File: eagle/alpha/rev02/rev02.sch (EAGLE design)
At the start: 382 parts, among them CN1 HOST, CN2 HOST, IC1 N25Q128A13ES, IC2 74AC244DW, IC3 N25Q128A13ES, J1 STM32-SWD, Q1 2N7002, Q2 BC818, Q4 2N7002, Q5 ASFL1, Q6 2N7002, T1 BC847, T2 BC847, U1 LMZ13608, U10 ATTINY828R-AU, U11 MC14551BDG, U12 23K640-I/SN, U13 XC7A200TFBG484, U14 EN6347QI, U15 EN6347QI, U16 EN5364QI, U2 LT3060ITS8-15, U3 MC74HC1G14DTT1G, U4 STM32F429BIT6, U5 IS45S32160F, U6 IS45S32160F, U7 MCP79412-I/SN, U8 FT232H_SERIAL, U9 FT232H_SERIAL, Y1 12 MHz, Y2 12 MHz

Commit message: First set of updates based on review feedback.
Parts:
- removed R17: 4.7k, resistor:R-EU_R0402
- C13, C7: value 2.2 uF -> 4.7 uF
- R24, R25, R28, R29: value 220 -> 330
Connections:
- removed net N$53: R4.2, U1.SYNC
- new net N$3: Q5.FO, R4.2
- net FPGA_GCLK: no longer Q5.FO
- net GND: now also C22.1, C23.1, C24.1, C25.1; no longer R17.1, R18.1, R4.1
- net KSM_PROM_CS_N: now also U4IO.PB0
- net VCCO_3V3: now also R18.1; no longer C22.1, C23.1, C24.1, C25.1, R17.2
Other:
- note added: "Connector for external 3V3 battery. Place a jumper between pins 1-2 to "emulate" having a battery present."
- note added: "NOTE: GPIO pins should be length matched to support I/O at XXX MHz (pavel)"
- note added: "NOTE: One of the FPGA_GPIO_* pins should be connected to one of the MRCC pins."
- note added: "XXX Add EEPROM for USB settings. Plan for now is to not populate it on the Alpha though."
- note removed: "Do we need more speed? Joachim expressed that we might need a faster interconnect to the Alpha than the 12 Mbaud the FT232H can deliver in UART mode (in an e-mail to tech@ 2015-08-18). An alternative is to connect all of the ADBUS (and more) to the ARM, and use one of the faster modes this chip supports (fastest: synchronous FT245 parallel FIFO at 40 Mbyte/s). Enabling the faster modes requires t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"
- note removed: "FPGA_GPIO_B* is blue LEDs in Alpha block diagram. Suggest pin header instead for more versatility."
- note removed: "Place a jumper between pins 1-2 to "emulate" having a battery present."
- note removed: "XXX EEPROM for USB settings or not?"
- moved on the sheet: C100, C101, C104, C113, C114, C115, C116, C117, C118, C119, C120, C123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

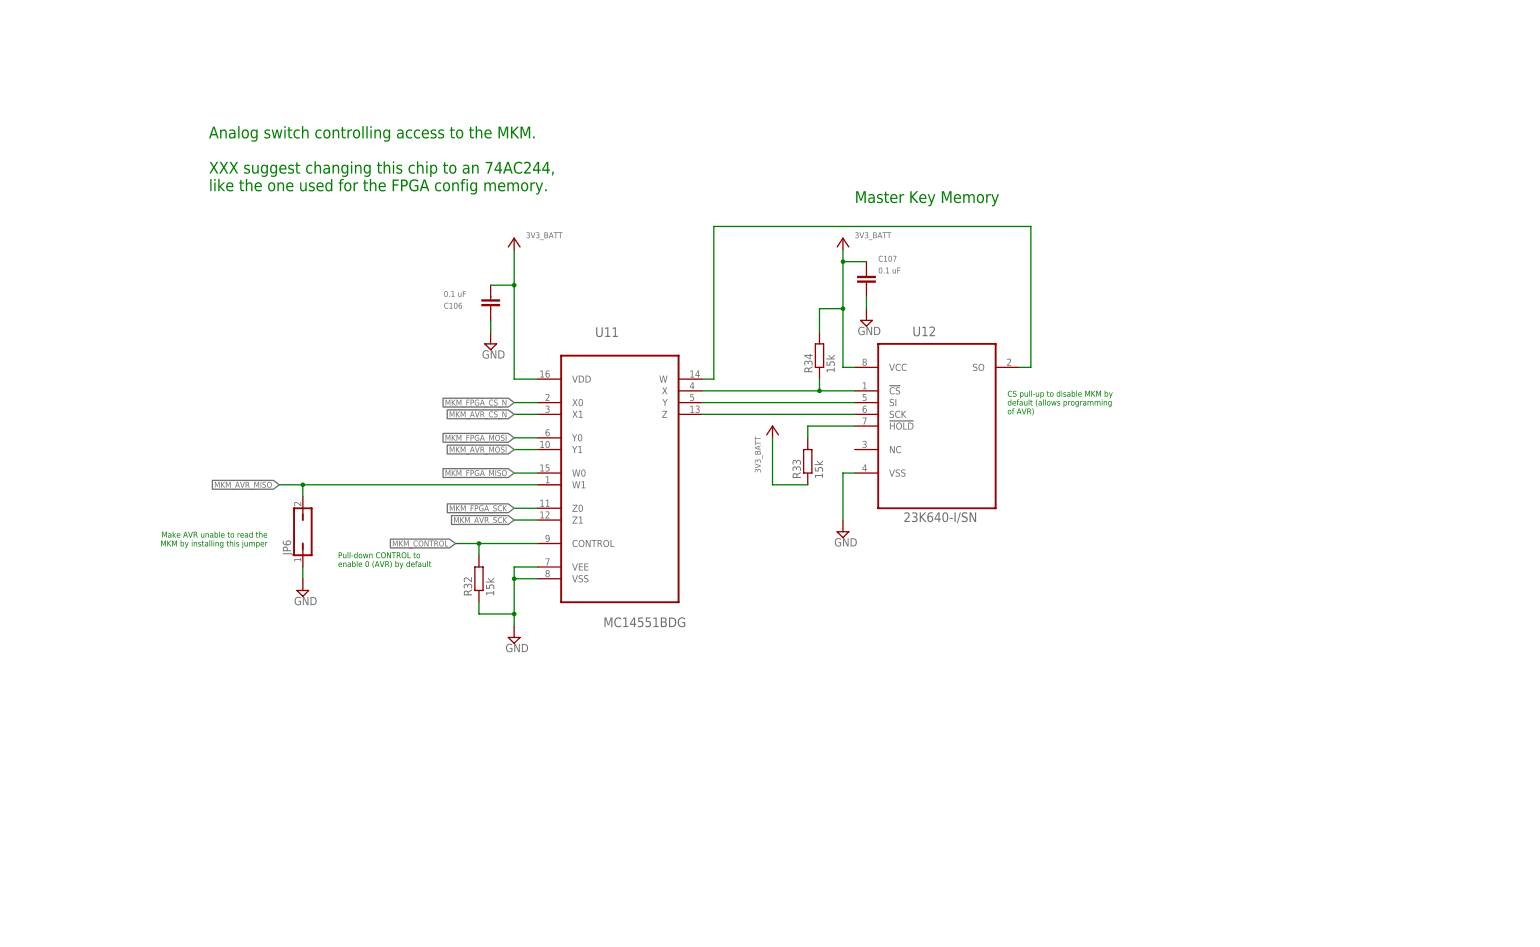
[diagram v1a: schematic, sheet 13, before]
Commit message: More schematic updates after review with Pavel.
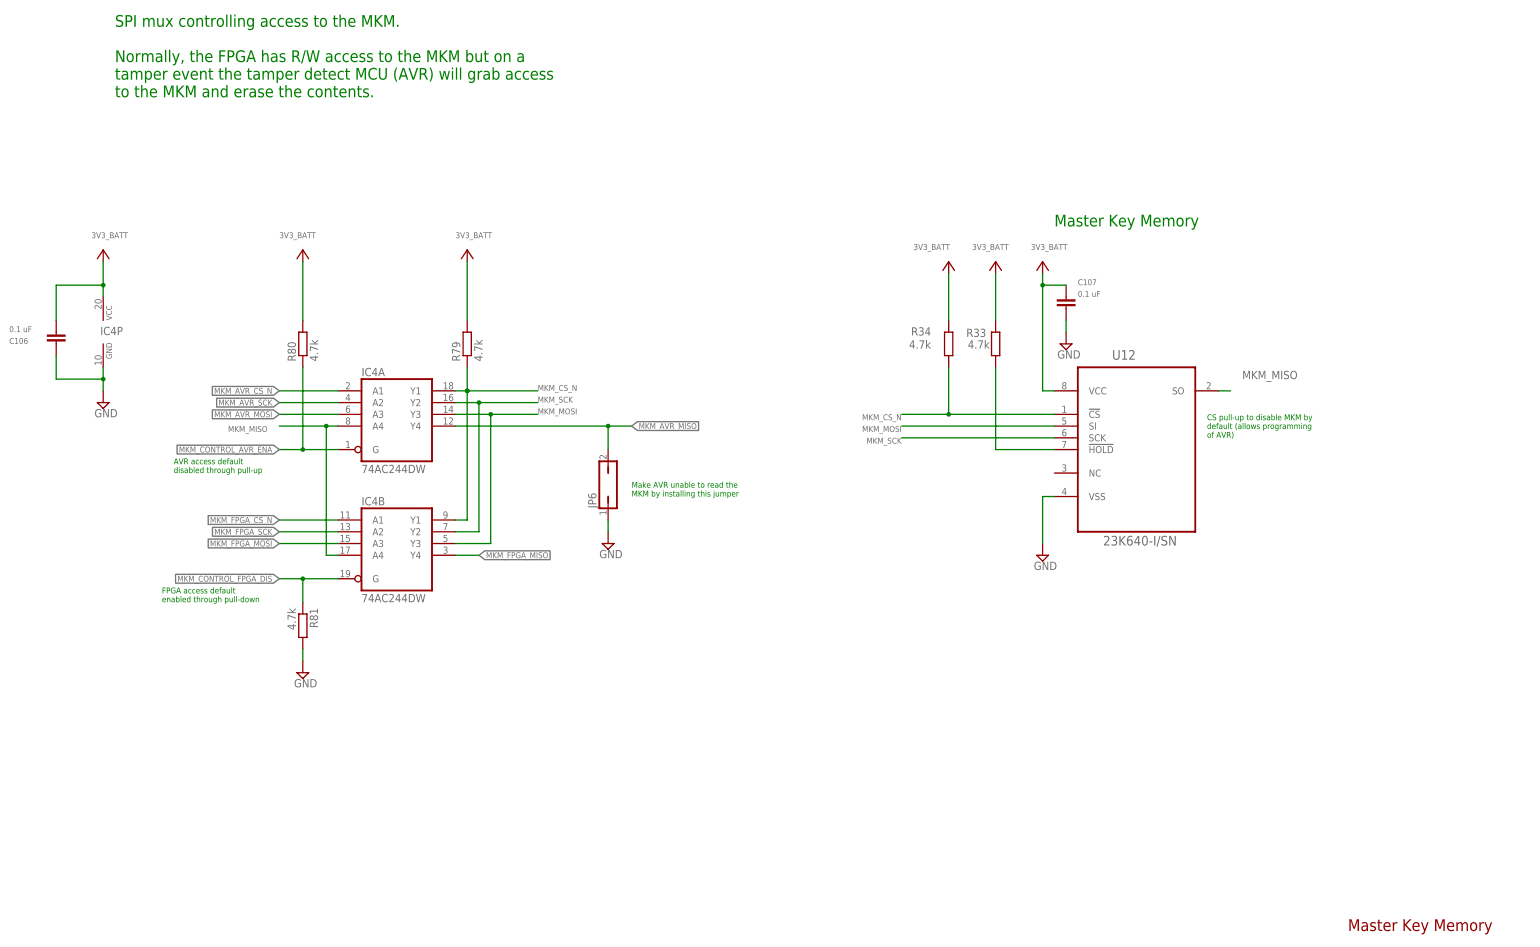
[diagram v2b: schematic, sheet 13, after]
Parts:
- removed U11: MC14551BDG, ON_Semiconductor-MC14551BDG:MC14551BDG
- added IC4: 74AC244DW, 74xx-eu:74AC244DW
- added R17, R79, R80, R81: 4.7k, resistor:R-EU_R0402
- added R82: 15k, resistor:R-EU_R0402
- R32: value 15k -> 0; TOLERANCE (none) -> 5%
- R33, R34: value 15k -> 4.7k
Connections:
- removed net AVR_GPIO_10: U10.PB2_(PCINT10/ADC10), U4IO.PC13
- removed net AVR_GPIO_11: U10.PB3_(PCINT11/ADC11), U4IO.PC14
- removed net AVR_GPIO_8: JP5.9, U10.(PCINT1/ADC1/AIN0)_PA1
- removed net FPGA_GPIO_TAMPER_0: U10.PB6_(PCINT14/ADC14), U13B16.IO_0_16
- removed net FPGA_GPIO_TAMPER_1: U10.PB7_(PCINT15/ADC15), U13B16.IO_L1P_T0_16
- removed net MKM_CONTROL: R32.2, U10.PC0_(PCINT16/ADC16/TOCC0/SS/XCK), U11.CONTROL
- removed net SDIO_CK: U4IO.SDIO_CK/PC12
- removed net SDIO_CMD: U4IO.SDIO_CMD/PD2
- removed net SDIO_D0: U4IO.SDIO_D0/PC8
- removed net SDIO_D1: U4IO.SDIO_D1/PC9
- removed net SDIO_D2: U4IO.SDIO_D2/PC10
- removed net SDIO_D3: U4IO.SDIO_D3/PC11
- new net AVR_GPIO_0: JP5.2, U10.PC0_(PCINT16/ADC16/TOCC0/SS/XCK)
- new net AVR_GPIO_ARM_0: U10.PB0_(PCINT8/ADC8), U4IO.PC13
- new net AVR_GPIO_ARM_1: U10.PB1_(PCINT9/ADC9), U4IO.PC14
- new net AVR_GPIO_FPGA_2: U10.PB6_(PCINT14/ADC14)
- new net AVR_GPIO_FPGA_3: U10.PB7_(PCINT15/ADC15)
- new net MKM_CONTROL_AVR_ENA: IC4A.G, R80.1, U10.(PCINT6/ADC6)_PA6
- new net MKM_CONTROL_FPGA_DIS: IC4B.G, R81.1
- new net N$23: IC1.!W!/VPP/DQ2, R17.2
- new net N$25: U4PWR.VBAT@6
- new net N$53: R32.2
- net 3V3_BATT: now also IC4P.VCC, R32.1, R79.2, R80.2, R82.2; no longer U11.VDD
- net AVR_GPIO_1: now also JP5.3, U10.PC1_(PCINT17/ADC17/TOCC1/INT0/CLKO); no longer JP5.2, U10.(PCINT18/ADC18/TOCC2/RXD/INT1)_PC2
- net AVR_GPIO_2: now also JP5.4, U10.(PCINT18/ADC18/TOCC2/RXD/INT1)_PC2; no longer JP5.3, U10.(PCINT19/ADC19/TOCC3/TXD)_PC3
- net AVR_GPIO_3: now also JP5.5, U10.(PCINT19/ADC19/TOCC3/TXD)_PC3; no longer JP5.4, U10.(PCINT20/ADC20/TOCC4)_PC4
- net AVR_GPIO_4: now also JP5.6, U10.(PCINT20/ADC20/TOCC4)_PC4; no longer JP5.5, U10.(PCINT21/ADC21/TOCC5/ICP1/T0)_PC5
- net AVR_GPIO_5: now also JP5.7, U10.(PCINT21/ADC21/TOCC5/ICP1/T0)_PC5; no longer JP5.6, U10.(PCINT22/ADC22/CLKI/TOCC6)_PC6
- net AVR_GPIO_6: now also JP5.8, U10.(PCINT22/ADC22/CLKI/TOCC6)_PC6; no longer JP5.7, U10.(PCINT23/ADC23/TOCC7/T1)_PC7
- net AVR_GPIO_7: now also JP5.9, U10.(PCINT23/ADC23/TOCC7/T1)_PC7; no longer JP5.8, U10.(PCINT0/ADC0)_PA0
- net AVR_LED1: now also U10.(PCINT0/ADC0)_PA0; no longer U10.(PCINT7/ADC7)_PA7
- net AVR_LED2: now also U10.(PCINT1/ADC1/AIN0)_PA1; no longer U10.(PCINT6/ADC6)_PA6
- net AVR_LED3: now also U10.(PCINT2/ADC2/AIN1)_PA2; no longer U10.(PC!INT5/ADC5)_PA5
- net AVR_LED4: now also U10.(PCINT3/ADC3)_PA3; no longer U10.(PCINT4/ADC4)_PA4
- net AVR_PANIC: now also R82.1; no longer U10.(PCINT2/ADC2/AIN1)_PA2
- net GND: now also IC4P.GND, R81.2; no longer R32.1, U11.VEE, U11.VSS
- net MKM_AVR_CS_N: now also IC4A.A1, U10.(PC!INT5/ADC5)_PA5; no longer U10.PC1_(PCINT17/ADC17/TOCC1/INT0/CLKO), U11.X1
- net MKM_AVR_MISO: now also IC4A.Y4; no longer U11.W1
- net MKM_AVR_MOSI: now also IC4A.A3; no longer U11.Y1
- net MKM_AVR_SCK: now also IC4A.A2; no longer U11.Z1
- net MKM_CS_N: now also IC4A.Y1, IC4B.Y1, R79.1; no longer U11.X
- net MKM_FPGA_CS_N: now also IC4B.A1; no longer U11.X0
- net MKM_FPGA_MISO: now also IC4B.Y4; no longer U11.W0
- net MKM_FPGA_MOSI: now also IC4B.A3; no longer U11.Y0
- net MKM_FPGA_SCK: now also IC4B.A2; no longer U11.Z0
- net MKM_MISO: now also IC4A.A4, IC4B.A4; no longer U11.W
- net MKM_MOSI: now also IC4A.Y3, IC4B.Y3; no longer U11.Y
- net MKM_SCK: now also IC4A.Y2, IC4B.Y2; no longer U11.Z
- net VCCO_3V3: now also R17.1; no longer IC1.!W!/VPP/DQ2, U4PWR.VBAT@6
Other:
- note added: "ARM I/O"
- note added: "ARM configuration"
- note added: "ARM power"
- note added: "AVR Tamper circuit"
- note added: "AVR access default disabled through pull-up"
- note added: "AVR_GPIO* AVR_LED* and AVR_PANIC can be swapped."
- note added: "FPGA CORE and AUX capacitors"
- note added: "FPGA CORE voltage regulators"
- note added: "FPGA FMC interface"
- note added: "FPGA GPIO"
- note added: "FPGA MKM interface"
- note added: "FPGA VCCO bypass capacitors"
- note added: "FPGA configuration interface"
- note added: "FPGA power and ground"
- note added: "FPGA power sequencing"
- note added: "FPGA supporting components"
- note added: "FPGA unused"
- note added: "FPGA unused banks"
- note added: "FPGA voltage regulators"
- note added: "Input power"
- note added: "Keystore memory"
- note added: "MGMT USB-UART"
- note added: "Noise source"
- note added: "SDRAM"
- note added: "SPI mux controlling access to the MKM. Normally, the FPGA has R/W access to the MKM but on a tamper event the tamper detect MCU (AVR) will grab access to the MKM and erase the contents."
- note added: "ST AN8844 §2.2 One bypass capacitor for every VDD. Use 0.1 uF X7R 10V."
- note added: "USB-UART interface"
- note removed: "AVR_GPIO* AVR_LED*, AVR_PANIC and FPGA_GPIO_TAMPER* can be swapped."
- note removed: "Analog switch controlling access to the MKM. XXX suggest changing this chip to an 74AC244, like the one used for the FPGA config memory."
- note removed: "Micro SD card goes here"
- note removed: "Pull-down CONTROL to enable 0 (AVR) by default"
- note removed: "Questions: 1) Which connector to use? Haven't found a good one with Eagle symbol. Some different kinds available. 2) Novena seems to have card reset capability (power control from MCU). Do we want the same? 3) Novena has two SD slots, and list power at 200mA. Do we need a separate power regulator for the SD card, or can we use VCCO_3V3?"
- note removed: "ST AN8844 §2.2 One bypass capacitor for every VDD. Use 0.1 uF X7R (X5R?) 10V."
- moved on the sheet: C102, C103, C104, C106, C107, C21, C70, C71, JP6, R19, R20, R21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

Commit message: Maybe final set of review feedback updates.
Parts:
- added C214, C215: 0.1 uF, resistor:C-EUC0402
- added FB5, FB6, FB7: 0, UsedComponents:BLM31PG330SN1_1206
- added IC5, IC6: RCLAMP0502ASC-89, UsedComponents:RCLAMP0502ASC-89
- added J2, J3: (no value), SparkFun-Connectors:M03X2NO_SILK
- added R83, R84, R85: 0, resistor:R-EU_R0603
- added R86, R87, R88, R89: 100, resistor:R-EU_R0402
- R62, R63, R71: device resistor:R-EU_R1206 -> resistor:R-EU_R0603; TOLERANCE (none) -> 5%
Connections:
- new net FPGA_CFG_CS_N1: R85.2, U13B14.IO_L6P_T0_FCS_B_14
- new net FPGA_CFG_MISO1: R84.2, U13B14.IO_L1N_T0_D01_DIN_14
- new net FPGA_CFG_MOSI1: R83.2, U13B14.IO_L1P_T0_D00_MOSI_14
- new net FPGA_CFG_SCLK1: R71.2, U13B0.CCLK_0
- new net FPGA_INIT_B_INT1: R62.2, U13B0.INIT_B_0
- new net FPGA_PROGRAM_B1: R63.2, U13B0.PROGRAM_B_0
- new net FT_MGMT_RXD1: R89.2
- new net FT_MGMT_TXD1: R88.2
- new net FT_RXD1: J2.4, J3.4, R87.2, U8.RXD
- new net FT_TXD1: J2.2, J3.2, R86.2, U8.TXD
- new net N$57: CN1.D+, IC5.IN1
- new net N$58: CN1.D-, IC5.IN2
- new net N$59: CN2.D+, IC6.IN1
- new net N$60: CN2.D-, IC6.IN2
- net FPGA_CFG_CS_N: now also R85.1; no longer U13B14.IO_L6P_T0_FCS_B_14
- net FPGA_CFG_MISO: now also R84.1; no longer U13B14.IO_L1N_T0_D01_DIN_14
- net FPGA_CFG_MOSI: now also R83.1; no longer U13B14.IO_L1P_T0_D00_MOSI_14
- net FPGA_CFG_SCLK: now also R71.1; no longer U13B0.CCLK_0
- net FPGA_INIT_B_INT: now also R62.1; no longer U13B0.INIT_B_0
- net FPGA_PROGRAM_B: now also R63.1; no longer U13B0.PROGRAM_B_0
- net FPGA_VCCAUX_1V8: now also FB5.2; no longer R62.2
- net FPGA_VCCINT_1V0: now also FB7.2; no longer R71.2
- net FT_MGMT_RXD: now also R89.1; no longer U9.RXD
- net FT_MGMT_TXD: now also R88.1; no longer U9.TXD
- net FT_MGMT_VREGIN: now also IC6.VCC
- net FT_RXD: now also R87.1; no longer U8.RXD
- net FT_TXD: now also R86.1; no longer U8.TXD
- net FT_VREGIN: now also IC5.VCC
- net GND: now also C214.2, C215.2, IC5.GND, IC6.GND, J2.6, J3.6
- net N$38: now also FB5.1; no longer R62.1
- net N$43: now also FB6.1; no longer R63.1
- net N$48: now also FB7.1; no longer R71.1
- net USB_DM: now also IC5.OUT2, J2.3, J3.3; no longer CN1.D-
- net USB_DP: now also IC5.OUT1, J2.5, J3.5; no longer CN1.D+
- net USB_MGMT_DM: now also IC6.OUT2; no longer CN2.D-
- net USB_MGMT_DP: now also IC6.OUT1; no longer CN2.D+
- net VCCO_3V3: now also C214.1, C215.1, FB6.2, J2.1, J3.1; no longer R63.2
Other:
- note added: "<-- Place small 0.47 uF caps right under the BGA package <-- Place medium 4.7 uF caps very close to the BGA package <-- Place large 47 uF caps not far from the BGA package <-- Place one of four 47 uF caps on every side of the BGA p. <-- Distribute six sets of caps among six FPGA I/O banks"
- note added: "If possible, line up with corresponding header for MGMT USB-UART and label pins on silk screen"
- note added: "If possible, line up with corresponding header for USB-UART and label pins on silk screen"
- note added: "NOTE: One of the FPGA_GPIO_* pins should be connected to one of the MRCC pins. The non-MRCC GPIO signals should be length matched to within 500 ps of the MRCC signal."
- note added: "These packages are TSSOP, but if new packages are to be created for layout, BGA package is preferred."
- note added: "This whole sheets circuitry should be as shielded as possible. Solid isolated ground plane and internal planes connected to the rest of the board at a single point is expected."
- note removed: "<-- Place small 0.47 uF caps right under the BGA package <-- Place medium 4.7 uF caps very close to the BGA package <-- Place large 47 uF caps not far from the BGA package <-- Place one of four 47 uF caps on every side of the BGA package <-- Distribute six sets of caps among six FPGA I/O banks"
- note removed: "Add optocoupler as per Jacob's suggestion on tech@ 2015-07-24? The suggestion is to add a fast optocoupler to really isolate AGND from GND. As this appears to require a bigger digitizer, we are reluctant to add that for the Alpha."
- note removed: "NOTE: GPIO pins should be length matched to support I/O at XXX MHz (pavel)"
- note removed: "NOTE: One of the FPGA_GPIO_* pins should be connected to one of the MRCC pins."
- note removed: "Should we keep this separate chip or rather connect VBAT to the STM32 and use the internal RTC?"
- note removed: "XXX Add EEPROM for USB settings. Plan for now is to not populate it on the Alpha though."
- moved on the sheet: C100, C101, C123, C124, C125, C126, C127, C128, C129, C130, C131, C132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

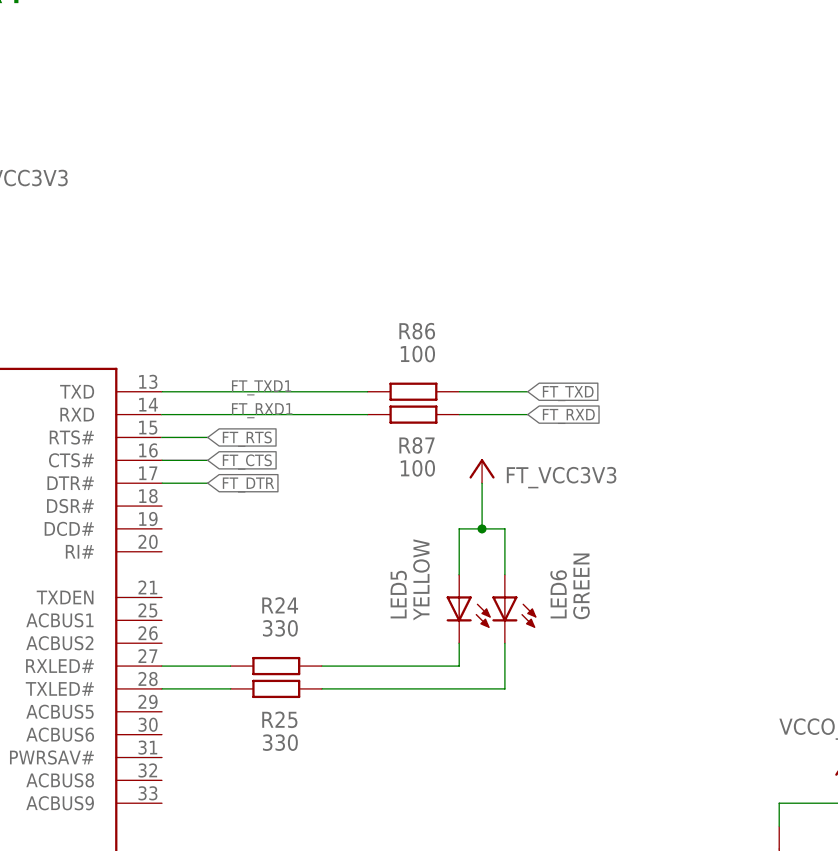
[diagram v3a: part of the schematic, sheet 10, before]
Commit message: Add FPGA part number and pull-ups to ARM UART RXs
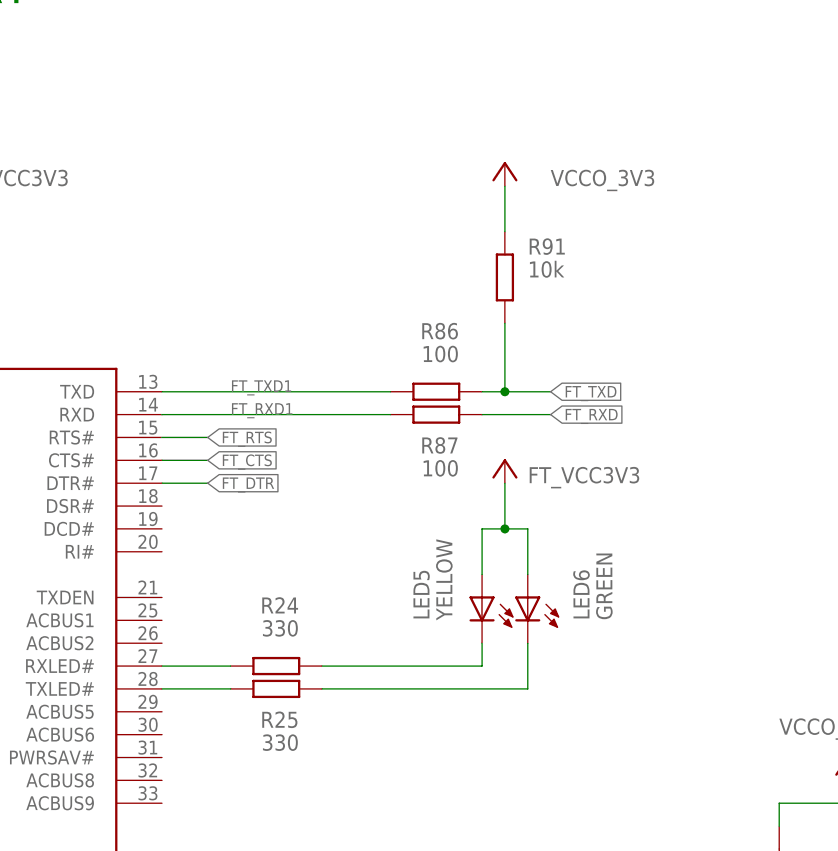
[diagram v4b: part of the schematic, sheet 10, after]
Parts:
- added R90, R91: 10k, resistor:R-EU_R0402
- U13: MFR (none) -> Xilinx; MPN (none) -> XC7A200T-1FBG484C; OC_DIGIKEY (none) -> 122-1871-ND
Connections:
- net FT_MGMT_TXD: now also R90.2
- net FT_TXD: now also R91.2
- net VCCO_3V3: now also R90.1, R91.1
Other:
- moved on the sheet: LED5, LED6, R86, R87
